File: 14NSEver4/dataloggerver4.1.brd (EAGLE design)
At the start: 81.3 x 25.4 mm, 46 parts, among them CN1 DM3AT, CN2 DM3AT, Q1 16mhz, Q2 16mhz

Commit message: changed board files
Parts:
- removed U$3: ATMEGA328P-AU, ATMAGA328P-AU:QFP80P900X900X120-32N
- added U$8: ATMEGA328P-AUATMEGA328P-AU, ATMEGA328P-AU:ATMEGA328P-AU
- U$1: value ATMEGA328P-AU -> ATMEGA328P-AUATMEGA328P-AU; device ATMAGA328P-AU:QFP80P900X900X120-32N -> ATMEGA328P-AU:ATMEGA328P-AU
- moved U$1 47.5 mm to (57.1, 15.2), flipped to the bottom, turned to 180 degrees
- moved JP2 44.1 mm to (11.4, 22.9), turned to 0 degrees
- moved U$2 43.8 mm to (44.5, 19.1), turned to 180 degrees
- moved BMX2 40.6 mm to (61.0, 0.00)
- moved CN1 40.2 mm to (10.2, 12.7), turned to 270 degrees
- moved R16 38.8 mm to (34.3, 3.81), flipped to the top
- moved L1 35.4 mm to (5.08, 25.4)
- moved R10 35.4 mm to (30.5, 3.81), flipped to the top, turned to 180 degrees
- moved SW1 34.7 mm to (26.7, 5.08)
- moved R15 34.2 mm to (49.5, 8.89), flipped to the top
- moved U$6 33.0 mm to (72.4, 26.7), turned to 180 degrees
- moved R14 32.1 mm to (45.7, 11.4), flipped to the top
- moved R12 29.5 mm to (8.89, 25.4)
- moved C3 29.3 mm to (30.5, 6.35), flipped to the top, turned to 0 degrees
- moved BMP1 28.5 mm to (36.8, 17.8), turned to 90 degrees
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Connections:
- removed net N$12: C1.1, Q1.1, U$1.PB6
- removed net N$13: C2.1, Q1.2, U$1.PB7
- new net N$16: C1.1, Q1.1, U$8.P$7
- new net N$17: C2.1, Q1.2, U$8.P$8
- new net RESETTB: U$4.5
- new net RESETTB1: U$7.5
- net +5V: now also U$1.P$18, U$1.P$4, U$1.P$6, U$8.P$18, U$8.P$4, U$8.P$6; no longer U$1.AVCC, U$1.VCC, U$1.VCC2, U$3.AVCC, U$3.VCC, U$3.VCC2
- net BORD1: now also U$8.P$1; no longer U$1.PD3
- net BORD2: now also U$8.P$32; no longer U$1.PD2
- net BORDRX: now also U$1.P$26; no longer U$3.PC3
- net BORDTX: now also U$1.P$25; no longer U$3.PC2
- net GND: now also U$1.P$21, U$1.P$3, U$1.P$5, U$4.1, U$7.1, U$8.P$21, U$8.P$3, U$8.P$5; no longer U$1.GND, U$1.GND2, U$1.GND3, U$3.GND, U$3.GND2, U$3.GND3, U$4.5, U$7.5
- net GPSRX: now also U$1.P$10; no longer U$3.PD6
- net GPSTX: now also U$1.P$11; no longer U$3.PD7
- net LED1.0: now also U$1.P$32; no longer U$3.PD2
- net LED1.1: now also U$1.P$1; no longer U$3.PD3
- net LED1.2: now also U$8.P$10; no longer U$1.PD6
- net LED1.3: now also U$8.P$11; no longer U$1.PD7
- net MISO: now also U$8.P$16; no longer U$1.PB4MISO
- net MISO1: now also U$1.P$16; no longer U$3.PB4MISO
- net MOSI: now also U$4.4, U$8.P$15; no longer U$1.PB3MOSI, U$4.3
- net MOSI1: now also U$1.P$15, U$7.4; no longer U$3.PB3MOSI, U$7.3
- net N$14: now also U$1.P$8; no longer U$3.PB7
- net N$3: now also U$1.P$7; no longer U$3.PB6
- net RESETB: now also U$8.P$29; no longer U$1.PC6RESET, U$4.1
- net RESETB1: now also U$1.P$29; no longer U$3.PC6RESET, U$7.1
- net RST: now also U$1.P$9; no longer U$3.PD5
- net RX: now also U$8.P$30; no longer U$1.PD0RX
- net RX1: now also U$1.P$30; no longer U$3.PD0RX
- net SCK: now also U$4.3, U$8.P$17; no longer U$1.PB5, U$4.4
- net SCK1: now also U$1.P$17, U$7.3; no longer U$3.PB5, U$7.4
- net SCL: now also U$8.P$28; no longer U$1.PC5SCL
- net SCL1: now also U$1.P$28; no longer U$3.PC5SCL
- net SDA: now also U$8.P$27; no longer U$1.PC4SDA
- net SDA1: now also U$1.P$27; no longer U$3.PC4SDA
- net SS: now also U$1.P$14, U$8.P$14; no longer U$1.PB2SS
- net SS1: no longer U$3.PB2SS
- net TX: now also U$8.P$31; no longer U$1.PD1TX
- net TX1: now also U$1.P$31; no longer U$3.PD1TX
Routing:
- net MISO: track 0.00 -> 27.6 mm
- net MOSI: track 0.00 -> 25.5 mm
- net SCK: track 0.00 -> 23.5 mm
- net N$16: track 0.00 -> 15.4 mm
- net N$3: track 0.00 -> 15.4 mm
- net RESETB: track 0.00 -> 14.9 mm
- net GPSTX: track 0.00 -> 14.6 mm
- net +5V: track 0.00 -> 13.9 mm
- net SDA: track 0.00 -> 13.3 mm, vias 0 -> 1
- net GPSRX: track 0.00 -> 12.8 mm
- net SCL: track 0.00 -> 12.6 mm, vias 0 -> 1
- net N$17: track 0.00 -> 12.0 mm
- net N$14: track 0.00 -> 11.2 mm
- net RST: track 0.00 -> 11.1 mm
- net SS1: track 0.00 -> 9.27 mm, vias 0 -> 1
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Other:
- board size 81.3 x 25.4 mm -> 81.3 x 29.2 mm

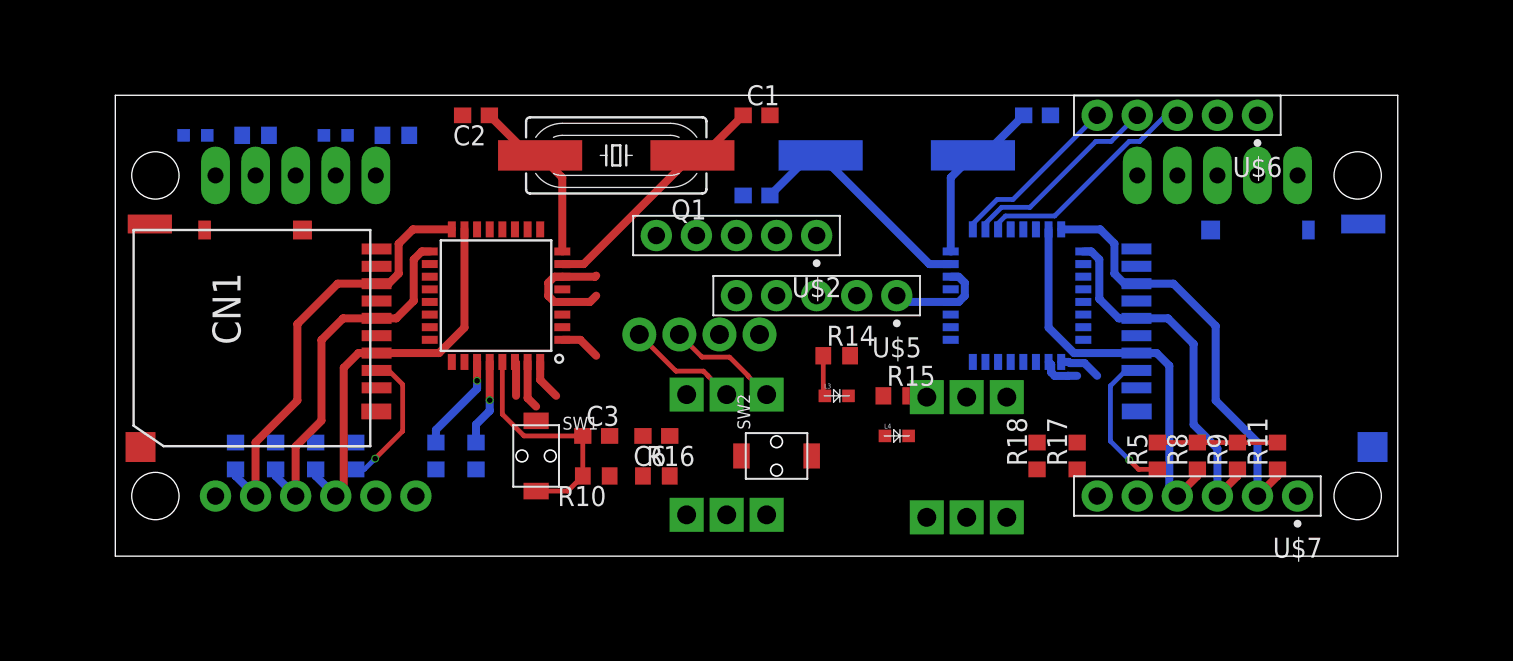
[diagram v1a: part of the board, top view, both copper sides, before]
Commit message: completed datalogger 4.1
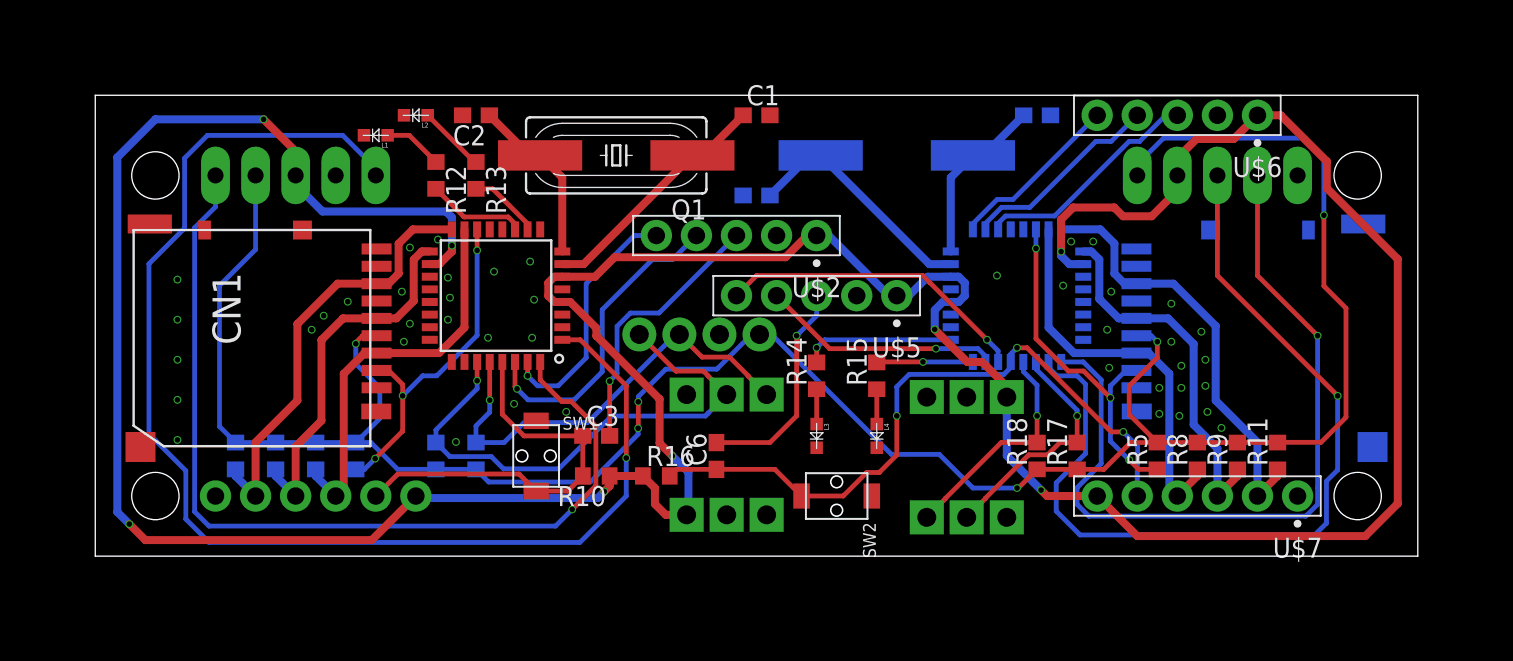
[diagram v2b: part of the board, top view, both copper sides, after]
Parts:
- moved R12 11.7 mm to (20.3, 22.9), flipped to the top, turned to 270 degrees
- moved L1 11.4 mm to (16.5, 25.4), flipped to the top, turned to 180 degrees
- moved R13 5.68 mm to (22.9, 22.9), flipped to the top, turned to 270 degrees
- moved L2 5.24 mm to (19.1, 26.7), flipped to the top, turned to 180 degrees
- moved SW2 4.58 mm to (45.7, 2.54), turned to 270 degrees
- moved C6 4.02 mm to (38.1, 5.08), turned to 90 degrees
- moved L3 2.84 mm to (44.5, 6.35), turned to 270 degrees
- moved R15 1.80 mm to (48.3, 10.2), turned to 90 degrees
- moved R14 1.80 mm to (44.5, 10.2), turned to 90 degrees
- moved L4 1.27 mm to (48.3, 6.35), turned to 270 degrees
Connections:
- removed net RESETTB: U$4.5
- removed net RESETTB1: U$7.5
- net RESETB: now also U$4.5
- net RESETB1: now also U$7.5
- net RX1: now also U$5.5; no longer U$5.4
- net SS: no longer U$1.P$14
- net SS1: now also U$1.P$14
- net TX1: now also U$5.4; no longer U$5.5
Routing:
- net +5V: track 13.9 -> 234.3 mm, vias 0 -> 8
- net +3V3: track 7.62 -> 150.1 mm, vias 0 -> 6
- net BORD1: track 2.57 -> 80.8 mm, vias 0 -> 1
- net BORD2: track 2.57 -> 58.4 mm, vias 0 -> 1
- net BORDRX: track 2.48 -> 55.5 mm, vias 0 -> 1
- net BORDTX: track 2.64 -> 49.8 mm, vias 0 -> 1
- net RESETB1: track 0.00 -> 43.2 mm, vias 0 -> 3
- net SDA: track 13.3 -> 34.4 mm
- net RX1: track 0.00 -> 19.8 mm, vias 0 -> 1
- net RX: track 2.18 -> 20.0 mm, vias 0 -> 1
- net RESET: track 0.00 -> 17.1 mm, vias 0 -> 1
- net SCL: track 12.6 -> 28.3 mm
- net TX1: track 0.00 -> 15.2 mm, vias 0 -> 1
- net SDA1: track 0.00 -> 15.2 mm, vias 0 -> 1
- net SCL1: track 0.00 -> 14.4 mm, vias 0 -> 1
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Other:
- board size 81.3 x 29.2 mm -> 83.8 x 29.2 mm

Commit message: completed ver4.1
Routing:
- net BORDRX: track 55.5 -> 54.8 mm
- net N$14: track 11.5 -> 10.9 mm

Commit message: changed v4.2
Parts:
- removed Q1, Q2: 16mhz, crystal:HC49UP
- added U$3, U$9: FE-238, FA-238:OSCCC300X230X120N
- moved C5 11.5 mm to (47.0, 25.4), turned to 0 degrees
- moved U$6 10.9 mm to (62.2, 22.9)
- moved C2 10.2 mm to (33.0, 25.4), turned to 0 degrees
- moved C1 7.18 mm to (35.6, 21.6)
- moved C4 3.81 mm to (44.5, 21.6)
- moved L2 2.84 mm to (21.6, 25.4)
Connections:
- net GND: now also U$3.GND, U$3.GND1, U$9.GND, U$9.GND1
- net N$14: now also U$9.3; no longer Q2.2
- net N$16: now also U$3.1; no longer Q1.1
- net N$17: now also U$3.3; no longer Q1.2
- net N$3: now also U$9.1; no longer Q2.1
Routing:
- net GPSTX: track 14.6 -> 3.92 mm
- net GPSRX: track 12.8 -> 3.96 mm
- net N$16: track 15.4 -> 8.18 mm
- net RST: track 11.1 -> 4.36 mm
- net N$3: track 15.4 -> 9.45 mm
- net N$1: track 4.29 -> 1.91 mm
- net N$17: track 10.9 -> 8.95 mm
- net N$14: track 10.9 -> 9.48 mm
- net +5V: track 234.5 -> 234.0 mm
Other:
- board size 83.8 x 29.2 mm -> 83.8 x 27.9 mm

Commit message: completed ver4.1
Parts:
- added U$10, U$11: F.T.E.LOGO, logo:LOGO
- moved BMP1 2.54 mm to (34.3, 17.8)
- moved U$5 0.38 mm to (49.5, 15.6)
- flipped U$4 to the top, turned to 0 degrees
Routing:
- net +5V: track 234.0 -> 245.5 mm
- net RESET: track 17.1 -> 20.5 mm
- net SDA: track 34.4 -> 36.9 mm
- net SCL: track 28.4 -> 29.7 mm
- net +3V3: track 150.4 -> 151.6 mm
- net RESET1: track 13.9 -> 14.6 mm
- net BORD1: track 80.6 -> 81.1 mm
- net TX: track 15.9 -> 15.4 mm
